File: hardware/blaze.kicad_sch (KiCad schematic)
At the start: 7 parts, among them J1 Conn_01x30, J2 Conn_01x02, J3 Conn_01x02, U1 Teensy4.0

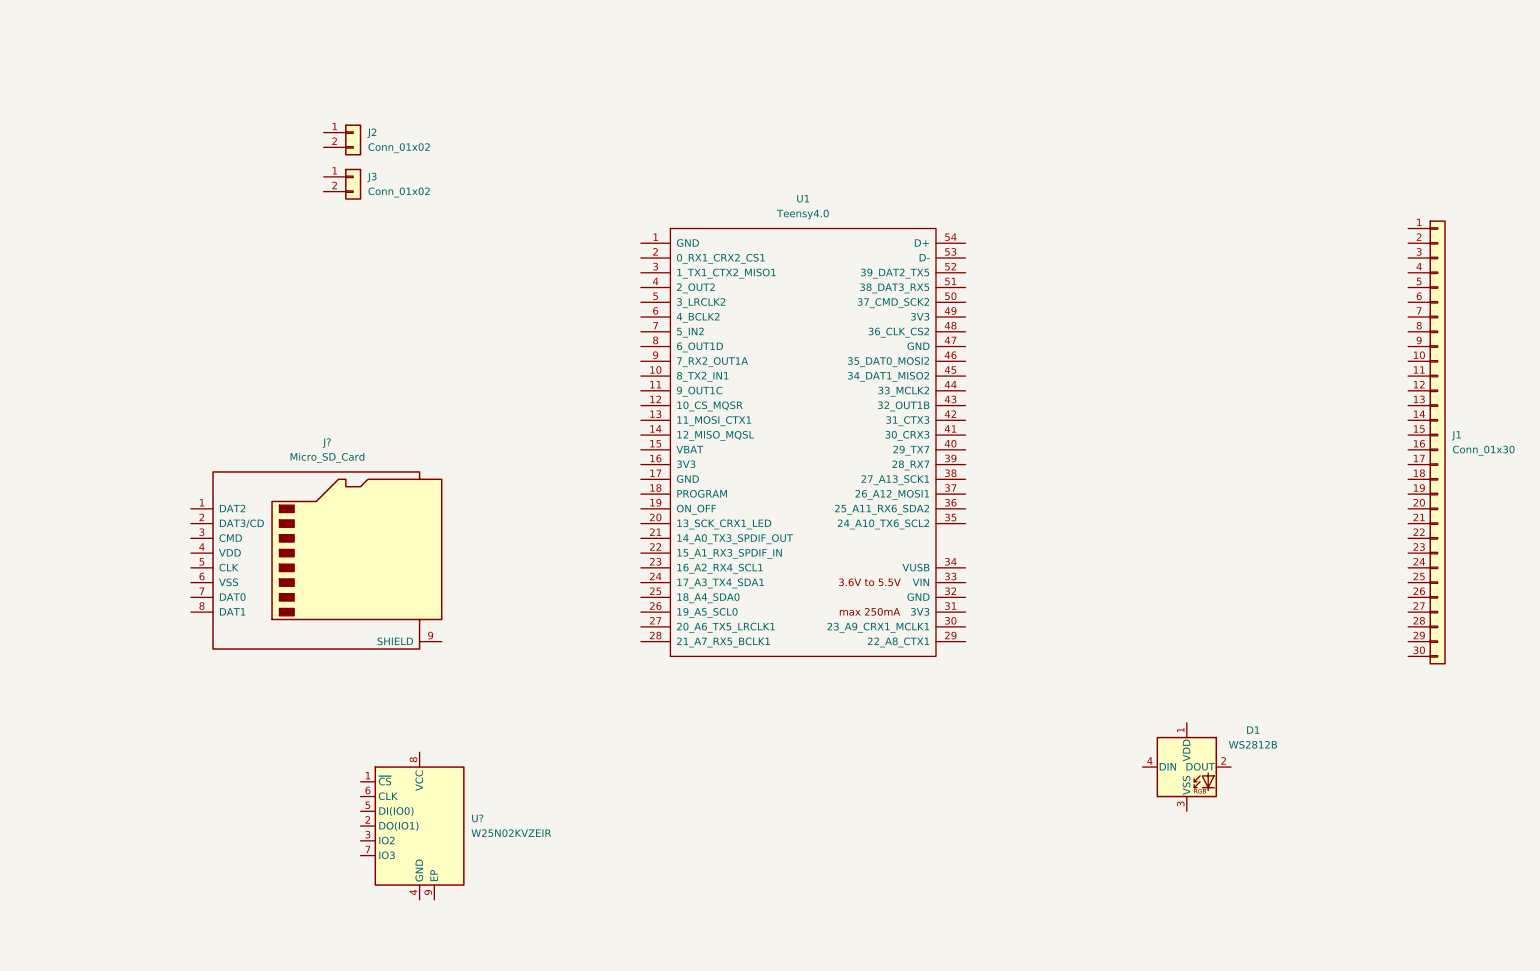
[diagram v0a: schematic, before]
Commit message: Power
Added power symbols and regulation
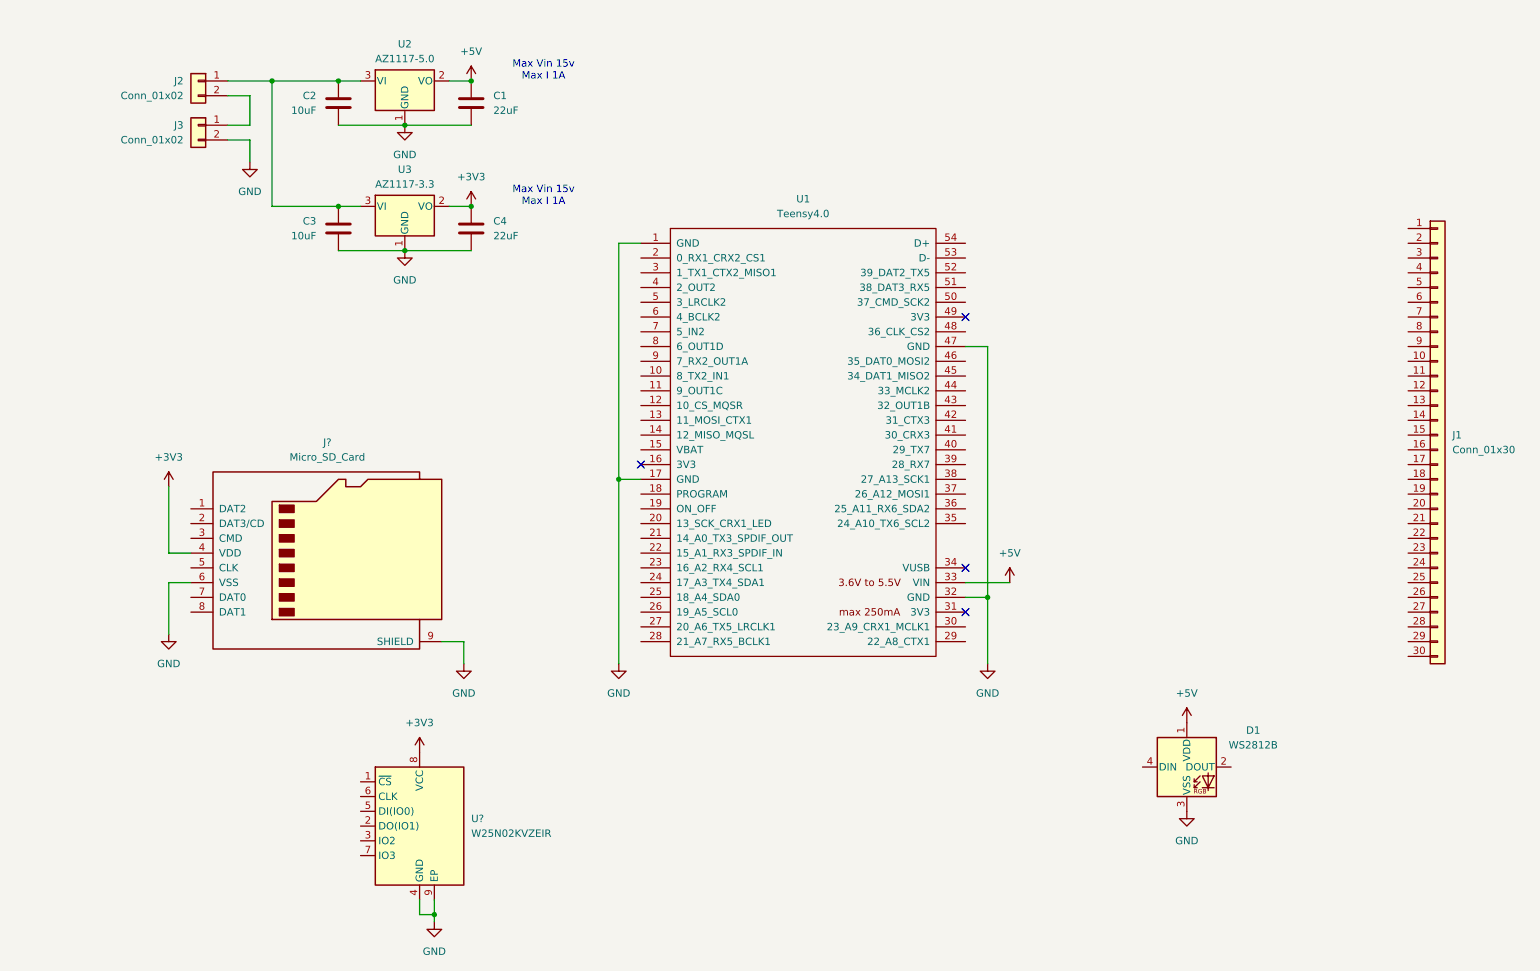
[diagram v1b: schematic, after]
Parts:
- added C1, C4: 22uF, symbol Device:C
- added C2, C3: 10uF, symbol Device:C
- added U2: AZ1117-5.0, Package_TO_SOT_SMD:SOT-223-3_TabPin2, symbol Regulator_Linear:AZ1117-5.0
- added U3: AZ1117-3.3, Package_TO_SOT_SMD:SOT-223-3_TabPin2, symbol Regulator_Linear:AZ1117-5.0
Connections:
- net GND: now reaches U?.4 (GND)
- net GND: now also D1.3 (VSS), J3.2 (Pin_2), J?.6 (VSS), J?.9 (SHIELD), U1.1 (GND), U1.17 (GND), U1.32 (GND), U1.47 (GND), U?.9 (EP), C1.2, C2.2, C3.2, C4.2, U2.1 (GND), U3.1 (GND)
- net +3V3: now reaches U?.8 (VCC)
- net +3V3: now also J?.4 (VDD), C4.1, U3.2 (VO)
- net +5V: now reaches D1.1 (VDD)
- net +5V: now also U1.33 (VIN), C1.1, U2.2 (VO)
- net at J3.1 (Pin_1): now also J2.2 (Pin_2)
- net at J2.1 (Pin_1): now also C2.1, C3.1, U2.3 (VI), U3.3 (VI)
- no-connect marks 0 -> 4
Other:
- note added: "Max Vin 15v Max I 1A"
- moved on the sheet: J2, J3

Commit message: Data Connections
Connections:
- net CS_FLASH: now reaches U?.1 (~{CS})
- net CS_FLASH: now also U1.12 (10_CS_MQSR)
- net MISO: now reaches U?.2 (DO(IO1))
- net MISO: now also J?.7 (DAT0), U1.14 (12_MISO_MQSL)
- net MOSI: now reaches U?.5 (DI(IO0))
- net MOSI: now also J?.3 (CMD), U1.13 (11_MOSI_CTX1)
- net SCK: now reaches U?.6 (CLK)
- net SCK: now also J?.5 (CLK), U1.20 (13_SCK_CRX1_LED)
- net LED_DOUT: now reaches D1.4 (DIN)
- net LED_DOUT: now also U1.8 (6_OUT1D)
- net CS_SD: now reaches J?.2 (DAT3/CD)
- net CS_SD: now also U1.11 (9_OUT1C)
- no-connect marks 4 -> 8

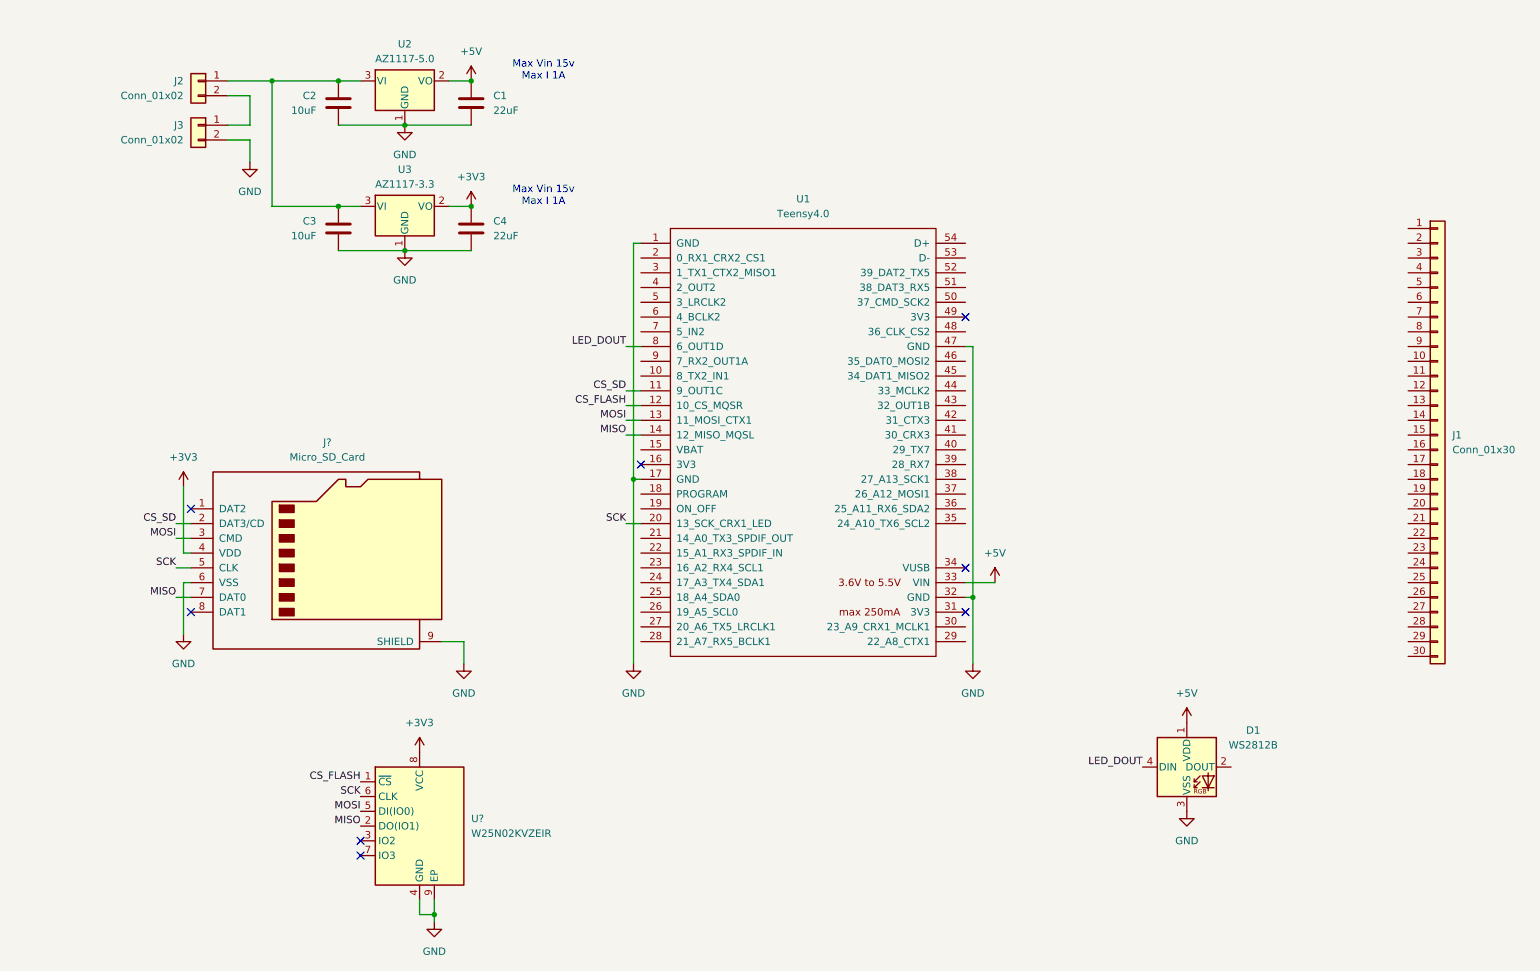
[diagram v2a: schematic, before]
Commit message: Decoupling and power
Added decoupling capacitors as well as other power protection features
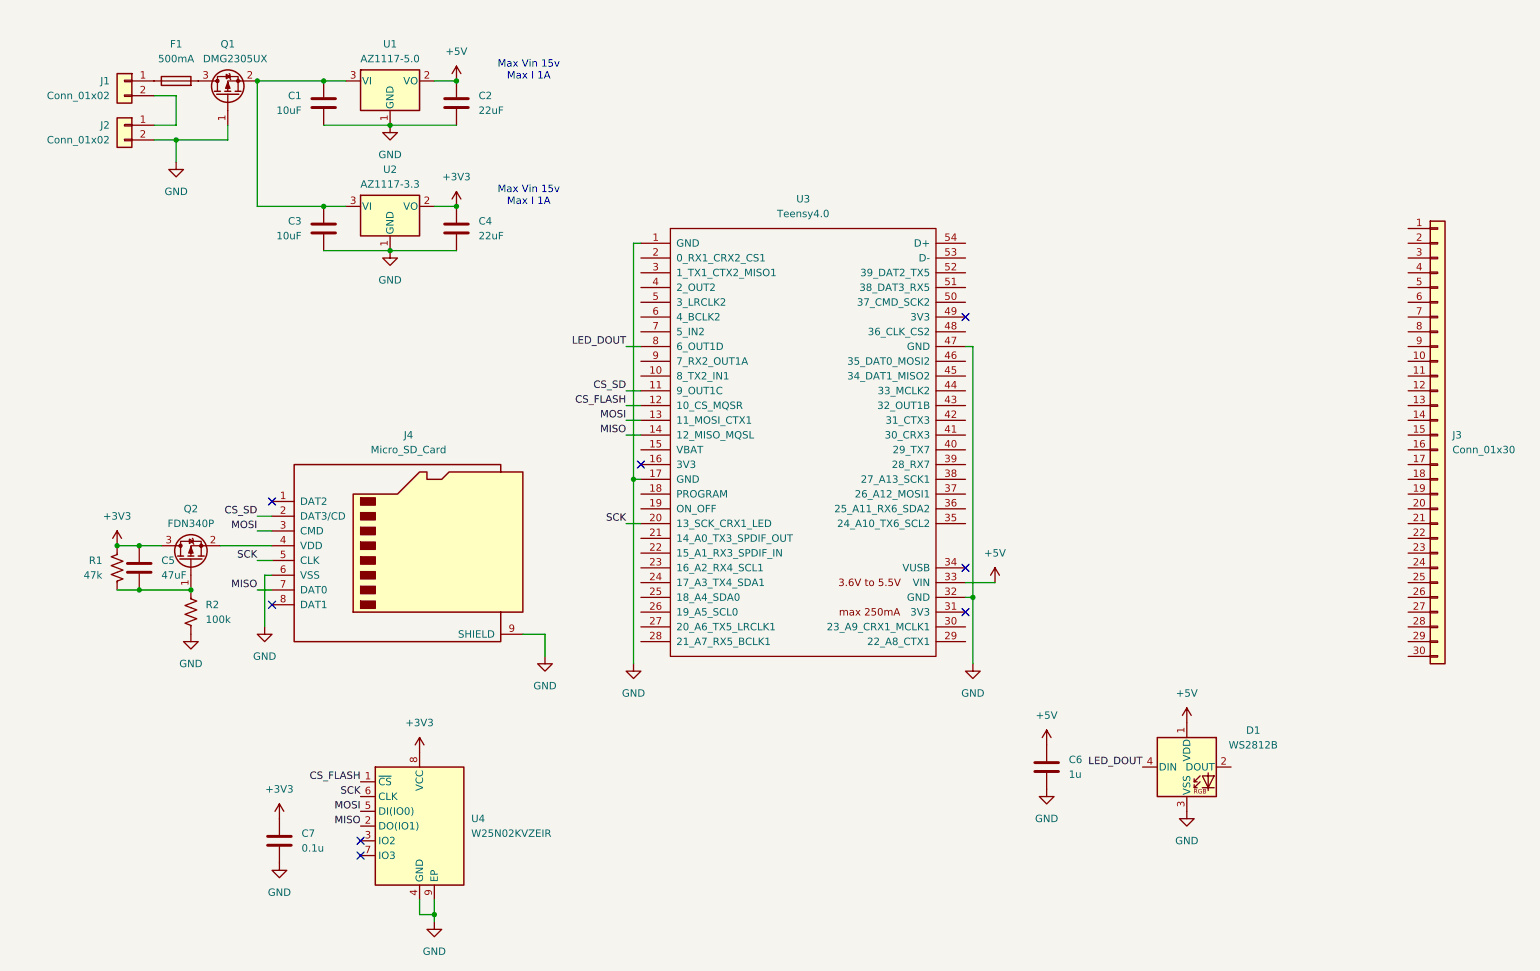
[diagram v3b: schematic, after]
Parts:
- added C5: 47uF, symbol Device:C
- added C6: 1u, symbol Device:C
- added C7: 0.1u, symbol Device:C
- added F1: 500mA, symbol Device:Fuse
- added Q1: DMG2305UX, Package_TO_SOT_SMD:SOT-23, symbol Transistor_FET:DMG2301L
- added Q2: FDN340P, Package_TO_SOT_SMD:SOT-23, symbol Transistor_FET:FDN340P
- added R1: 47k, symbol Device:R_US
- added R2: 100k, symbol Device:R_US
- gave numbers to parts that had none: 2
- renumbered C2 to C1, C1 to C2, J2 to J1, J3 to J2, J1 to J3, U2 to U1, U3 to U2, U1 to U3
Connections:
- net +3V3: now also C5.1, C7.1, Q2.3 (D), R1.1; no longer J4.4 (VDD)
- net +5V: now also C6.1
- net GND: now also C6.2, C7.2, Q1.1 (G), R2.2
- net at C1.1, C3.1, U1.3 (VI)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: now also Q1.2 (S); no longer J1.1 (Pin_1)
- new net: C5.2, Q2.1 (G), R1.2, R2.1
- new net: J4.4 (VDD), Q2.2 (S)
- new net: F1.2, Q1.3 (D)
- new net: F1.1, J1.1 (Pin_1)
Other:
- moved on the sheet: C1, C2, C3, C4, J1, J2, J4, U1, U2

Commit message: Added current sensing
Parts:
- added C8: 0.1u, symbol Device:C
- added J5: Conn_01x03_Pin, symbol Connector:Conn_01x03_Pin
- added R3, R4: 0.02, symbol Device:R_US
- added U5: ~, symbol Blaze_Lib:INA2181
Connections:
- net +3V3: now also C8.1, R4.2, U5.10 (VS), U5.8 (IN-2); no longer C4.1, U2.2 (VO)
- net +5V: now also J5.3 (Pin_3), R3.2, U5.2 (IN-1); no longer C2.1, U1.2 (VO)
- net GND: now also C8.2, J5.1 (Pin_1), U5.11 (PAD), U5.4 (GND), U5.5 (REF1), U5.6 (REF2)
- net at D1.2 (DOUT): now also J5.2 (Pin_2)
- net 5V_SENSE: now reaches U3.21 (14_A0_TX3_SPDIF_OUT)
- net 5V_SENSE: now also C2.1, U1.2 (VO), R3.1, U5.1 (OUT1)
- net 3V3_SENSE: now reaches U3.22 (15_A1_RX3_SPDIF_IN)
- net 3V3_SENSE: now also C4.1, U2.2 (VO), R4.1, U5.9 (OUT2)
- new net 3V3_SENSE_IN: U5.7 (IN+2)
- new net 5V_SENSE_IN: U5.3 (IN+1)
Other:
- note added: "These resistors must dissipate 1/2W"
- title: (none) -> Blaze Brain

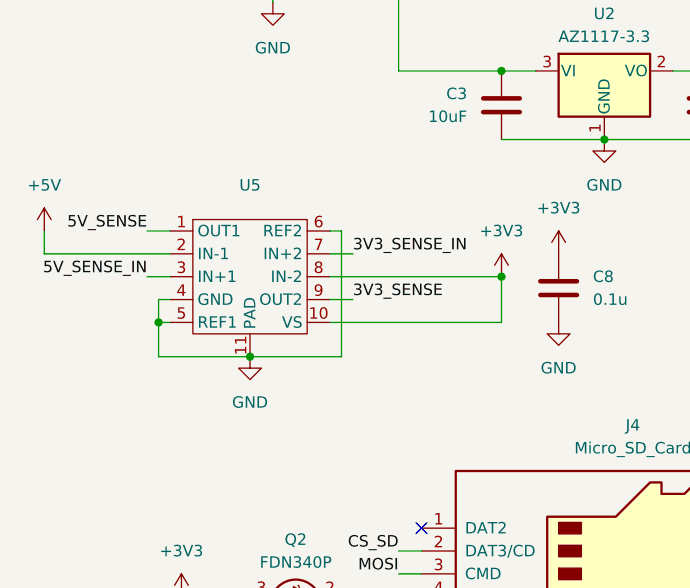
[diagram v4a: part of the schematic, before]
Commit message: Updated UNA2181 symbol
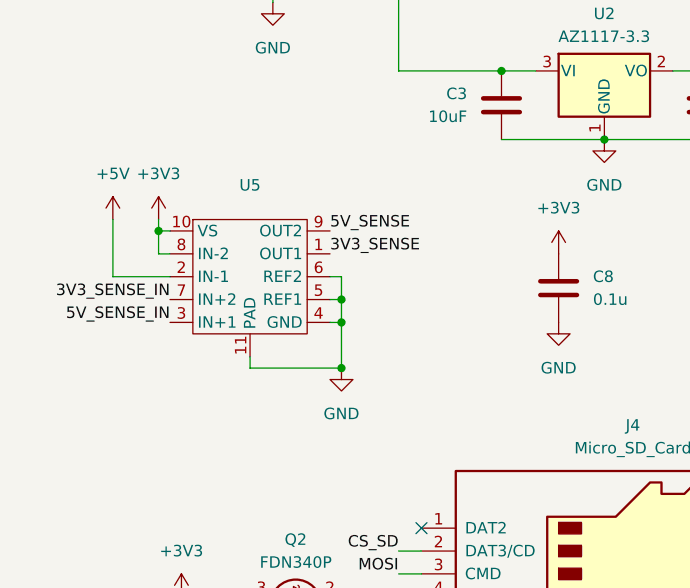
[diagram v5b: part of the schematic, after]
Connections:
- net 3V3_SENSE: now also U5.1 (OUT1); no longer U5.9 (OUT2)
- net 5V_SENSE: now also U5.9 (OUT2); no longer U5.1 (OUT1)
